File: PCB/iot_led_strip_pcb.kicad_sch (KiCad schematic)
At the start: 42 parts, among them J1 Screw_Terminal_01x03, J2 Screw_Terminal_01x03, J3 GT-USB-7010ASV, J4 Barrel_Jack_Switch_Pin3Ring, J5 TC2050-JTAG, SW1 RESET, SW2 FLASH, SW3 SW_SPDT, SW4 SW_SPDT, U3 ESP32-S2-SOLO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

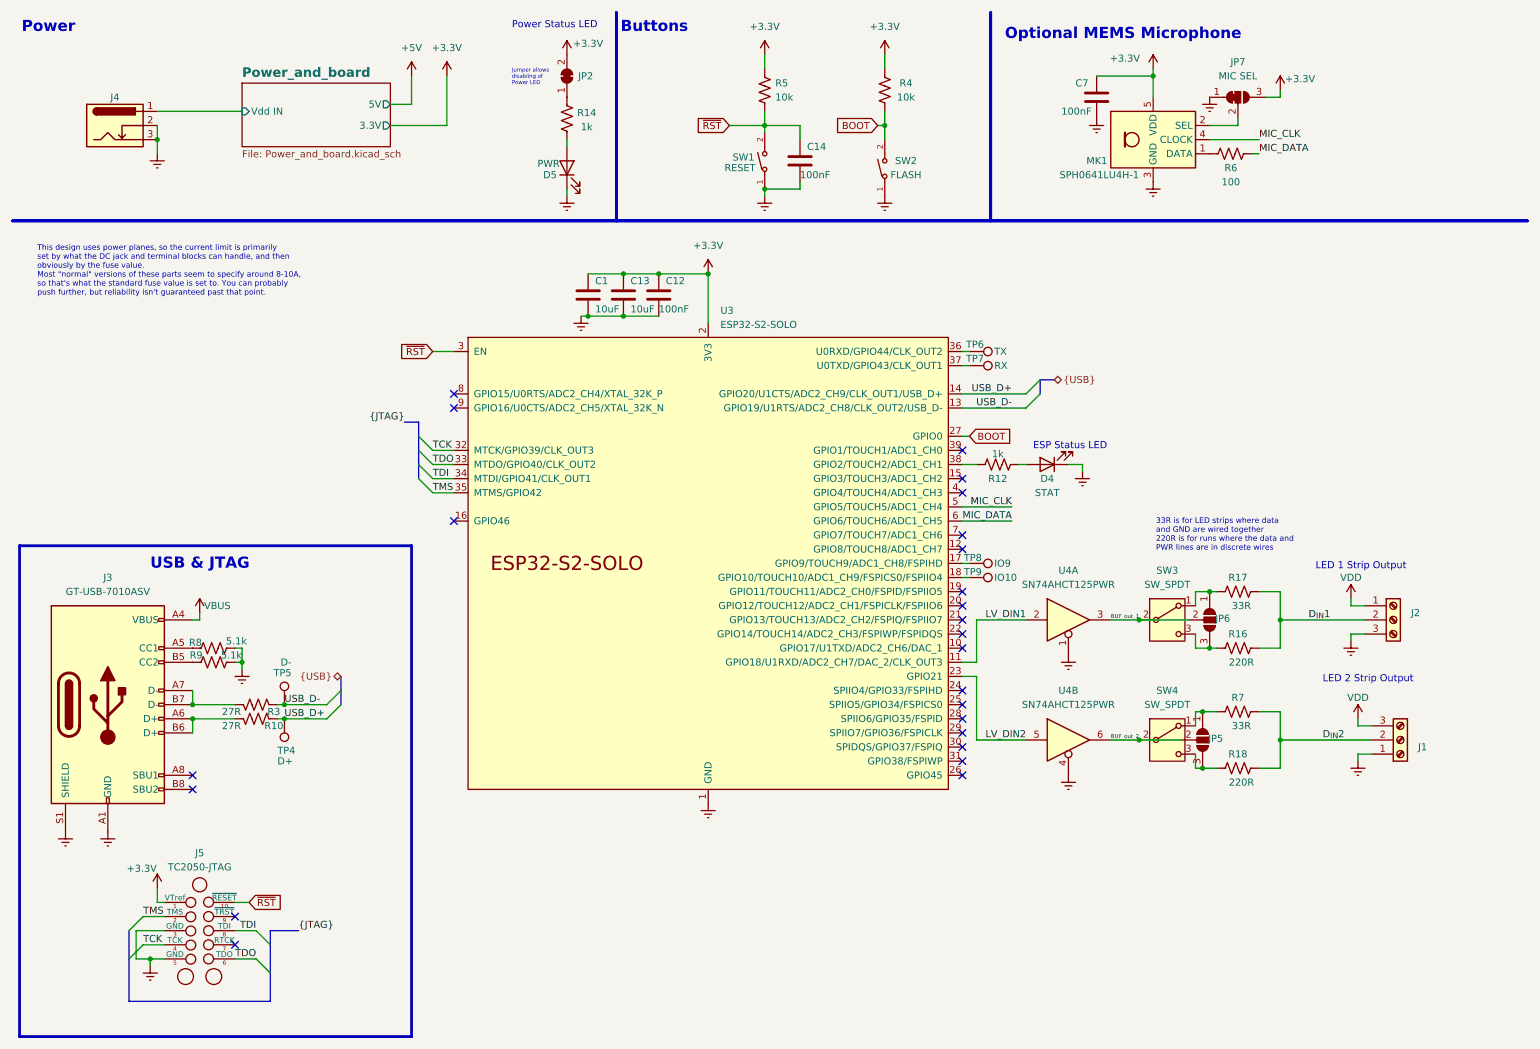
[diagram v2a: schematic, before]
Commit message: v3.2 changes
* Removed PTC fuse, since that caused issues on the last one
* Other minor changes (that i've forgotten)
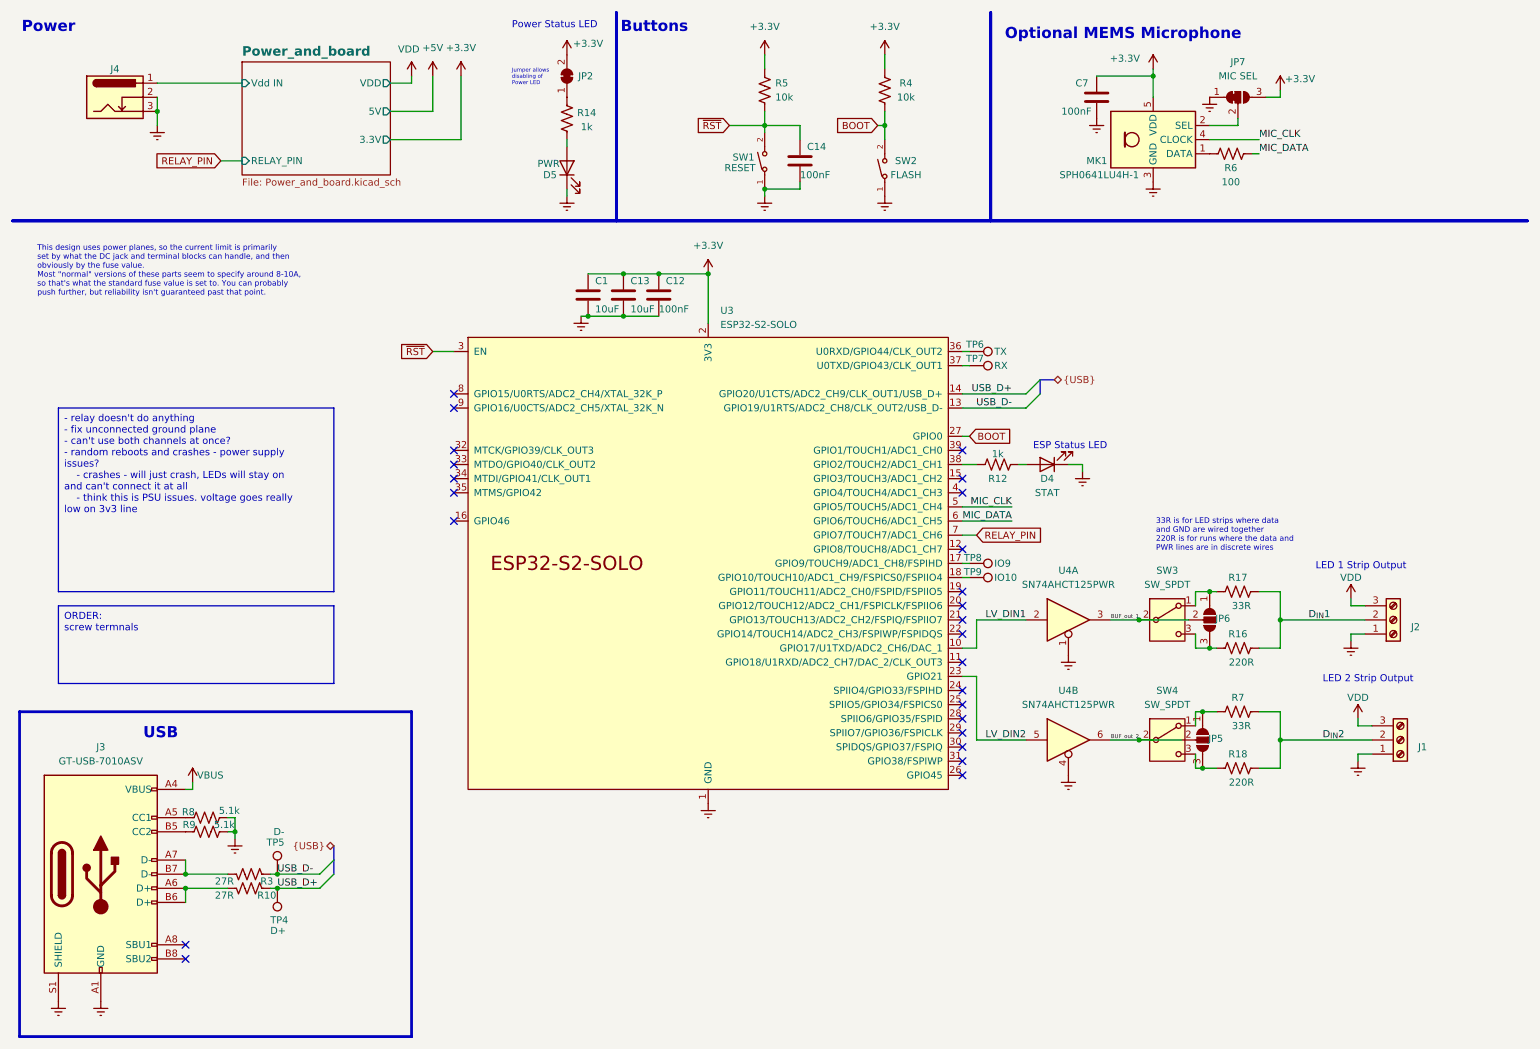
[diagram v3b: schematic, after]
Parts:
- removed J5: TC2050-JTAG, jmux-footprints:Tag-Connect_TC2050-IDC-FP_2x05_P1.27mm_Vertical, symbol jmux-kicadlib:TC2050-JTAG
- J1, J2: LCSC (none) -> C5188425; Note (none) -> not tried yet, but should be good; Vendor (none) -> https://www.lcsc.com/product-detail/Screw-Terminal-Blocks_M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
- J3: value GT-USB-7010ASV -> GT-USB-7010ASV
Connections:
- net Earth: now also J2.1 (Pin_1); no longer J2.3 (Pin_3)
- net LV_DIN1: now also U3.10 (GPIO17/U1TXD/ADC2_CH6/DAC_1); no longer U3.11 (GPIO18/U1RXD/ADC2_CH7/DAC_2/CLK_OUT3)
- net VDD: now also J2.3 (Pin_3); no longer J2.1 (Pin_1)
- net RELAY_PIN: now reaches U3.7 (GPIO7/TOUCH7/ADC1_CH6)
- net TCK: no longer names the net of U3.32 (MTCK/GPIO39/CLK_OUT3)
- net TDI: no longer names the net of U3.34 (MTDI/GPIO41/CLK_OUT1)
- net TDO: no longer names the net of U3.33 (MTDO/GPIO40/CLK_OUT2)
- net TMS: no longer names the net of U3.35 (MTMS/GPIO42)
- no-connect marks 24 -> 25
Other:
- sheet Power_and_board ports: added RELAY_PIN, VDD; removed none
- note added: "USB"
- note removed: "USB & JTAG"
- moved on the sheet: J3, J4, R10, R3, R8, R9, TP4, TP5
